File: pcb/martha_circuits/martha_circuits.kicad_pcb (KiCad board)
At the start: 2 copper layers, 11 parts, among them J1 Conn_01x06, J2 Conn_01x06, J3 Conn_01x06, J4 Conn_01x06, J5 IMU, U5 LM339

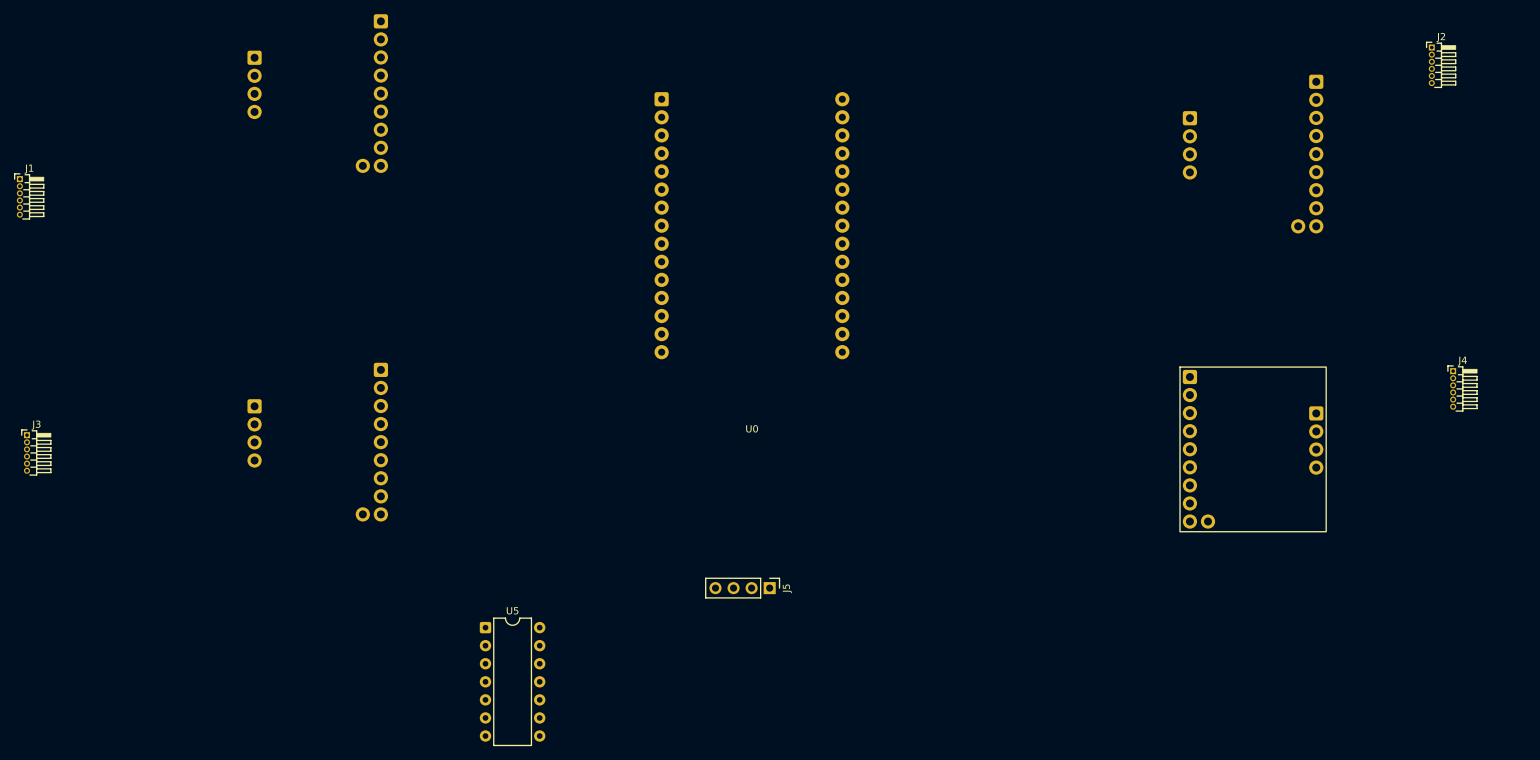
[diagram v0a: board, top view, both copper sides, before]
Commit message: Component rearrangement, and use of power symbols to reduce wiring in schematic. Add Deans connector footprint
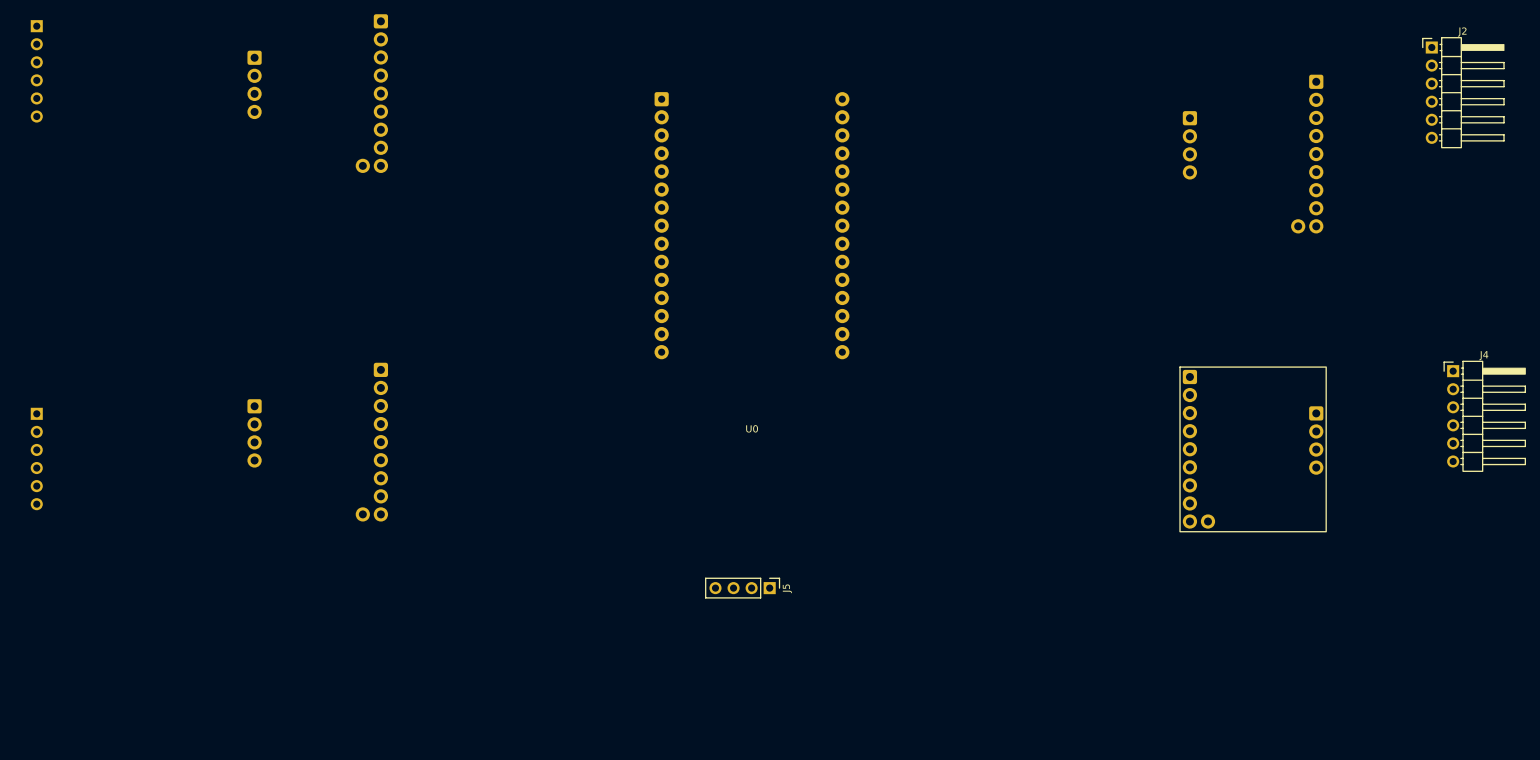
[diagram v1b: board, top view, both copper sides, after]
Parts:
- removed U5: LM339, Package_DIP:DIP-14_W7.62mm
- J1, J3: footprint Connector_PinHeader_1.00mm:PinHeader_1x06_P1.00mm_Horizontal -> Connector_PinHeader_2.54mm:PinHeader_1x06_P2.54mm_Horizontal; moved to B.Cu
- J2, J4: footprint Connector_PinHeader_1.00mm:PinHeader_1x06_P1.00mm_Horizontal -> Connector_PinHeader_2.54mm:PinHeader_1x06_P2.54mm_Horizontal
- moved J1 21.6 mm to (49.5, 72.0), turned to 180 degrees
- moved J3 3.30 mm to (49.5, 126.5), turned to 180 degrees
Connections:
- J2 pad 3: Net-(J2-Pin_3) -> Net-(J1-Pin_3)
- J2 pad 5: Net-(J2-Pin_5) -> unconnected-(J2-Pin_5-Pad5)
- J2 pad 6: Net-(J2-Pin_6) -> unconnected-(J2-Pin_6-Pad6)
- J4 pad 3: Net-(J2-Pin_3) -> Net-(J1-Pin_3)
- J4 pad 5: Net-(J4-Pin_5) -> unconnected-(J4-Pin_5-Pad5)
- J4 pad 6: Net-(J4-Pin_6) -> unconnected-(J4-Pin_6-Pad6)
- J5 pad 2: Net-(J2-Pin_3) -> Net-(J1-Pin_3)
- U0 pad 17: Net-(J2-Pin_3) -> Net-(J1-Pin_3)
- U0 pad 2: Net-(J2-Pin_5) -> unconnected-(U0-VP(36)-Pad2)
- U0 pad 24: Net-(J4-Pin_5) -> unconnected-(U0-D18-Pad24)
- U0 pad 25: Net-(J4-Pin_6) -> unconnected-(U0-D19-Pad25)
- U0 pad 3: Net-(J2-Pin_6) -> unconnected-(U0-VN(39)-Pad3)
- U2 pad 2: Net-(J2-Pin_3) -> Net-(J1-Pin_3)
- U4 pad 2: Net-(J2-Pin_3) -> Net-(J1-Pin_3)
